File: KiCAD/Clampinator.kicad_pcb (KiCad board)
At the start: 4 copper layers, 200 x 115 mm, 197 parts, among them J1 Power, J10 Conn_01x04, J11 Conn_01x04, J12 FDCAN_1, J13 FDCAN_2, J14 10k NTC, J15 10k NTC, J16 EN_NTC_B, J17 EN_NTC_A, J18 FAN, J19 FAN, J20 VP0265840000G, J23 VP0265840000G, J24 VP0265840000G, J25 +5V INJ, J26 UART4, J5 Debug Header, J6 Conn_01x04, J7 Conn_01x04, J8 Conn_01x04, J9 Conn_01x04, Q1 TK100E10N1,S1X, Q10 AO3400A, Q2 TK100E10N1,S1X, Q3 TK100E10N1,S1X, Q4 TK100E10N1,S1X, Q5 TK100E10N1,S1X, Q9 MMBT3904-C20526, SW1 PTS810SJM250SMTRLFS, SW2 PTS810SJM250SMTRLFS, SW3 PTS810SJM250SMTRLFS, SW4 PTS810SJM250SMTRLFS, SW5 SMQS-02R-TP, SW6 EG1847-ND, SW7 GPI-154-3013, U1 STM32H573RIT6, U10 LM74810QDRRRQ1, U12 TPS7A2033DQNR, U13 VOS618A-3T, U14 LM5163DDAR, U2 TL432BQDBZR, U3 EG2131, U4 UCC33420RAQR_C46461551, U5 USBLC6-2SC6, U6 LM5012DDAR, U7 MCP2562FD-E/P, U8 MCP2562FD-E/P, U9 EL357N, X1 SC-32S32.768kHz20PPM7pF, Y2 ECS-80-18-23B-JTM-TR

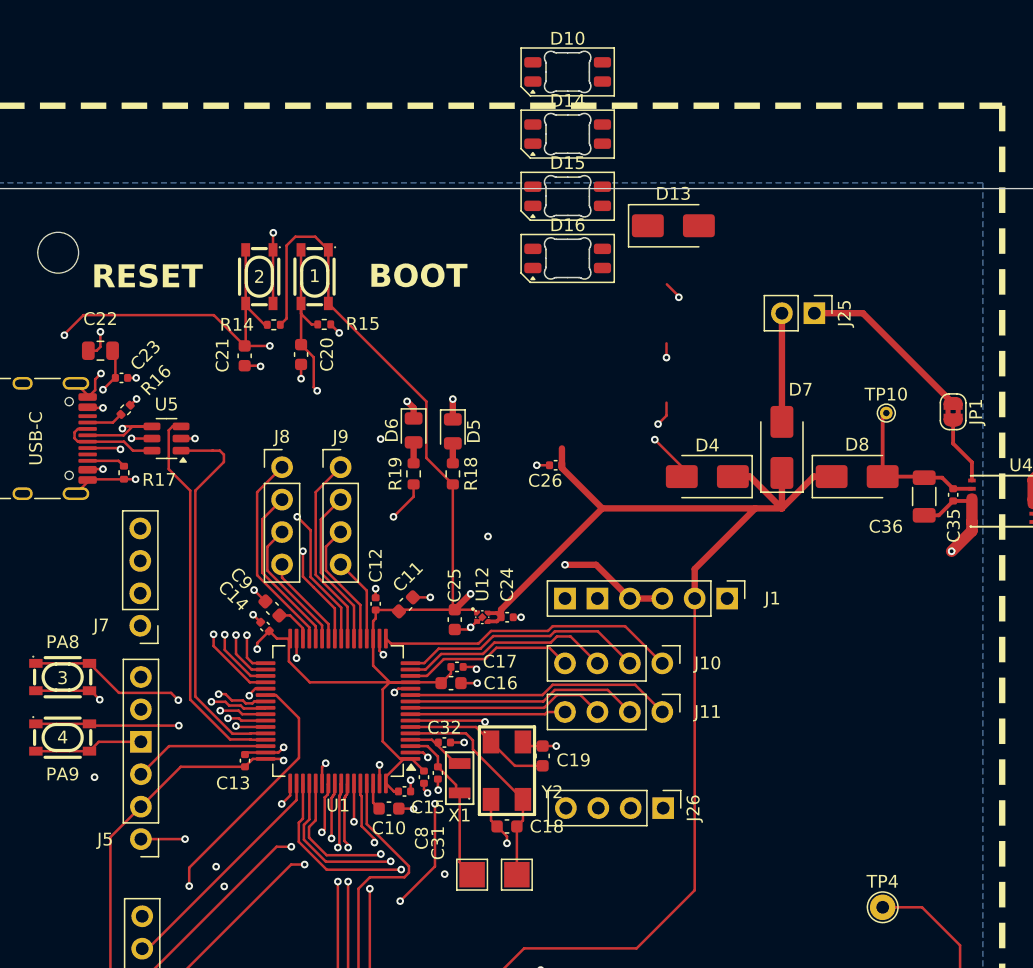
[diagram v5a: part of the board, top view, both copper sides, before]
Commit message: Finish SK7812 layouts + new forward mount footprint from reverse extended leads footprint
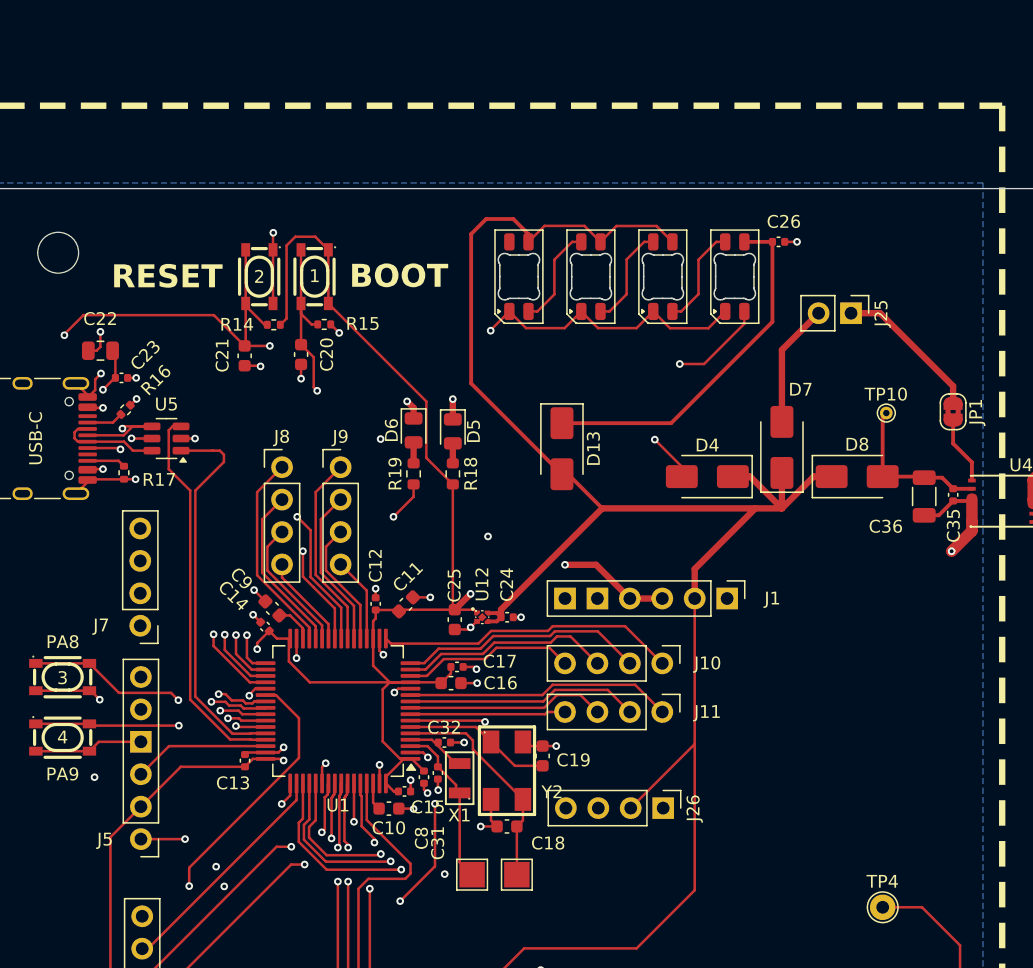
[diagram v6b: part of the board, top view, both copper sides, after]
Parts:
- D10, D14, D15, D16: footprint LED_SMD:LED_SK6812MINI-E_3.2x2.8mm_P1.5mm_ReverseMount -> LED_SMD:LED_SK6812MINI-E_3.2x2.8mm_P1.5mm
- moved C26 24.7 mm to (109.3, 28.7), turned to 0 degrees
- moved D10 20.7 mm to (105.8, 31.4), turned to 90 degrees
- moved D13 19.5 mm to (92.3, 44.9), turned to -90 degrees
- moved D14 13.4 mm to (100.2, 31.4), turned to 90 degrees
- moved D15 6.56 mm to (94.6, 31.4), turned to 90 degrees
- moved D16 4.08 mm to (88.9, 31.4), turned to 90 degrees
- moved J25 2.88 mm to (114.9, 34.3)
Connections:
- C26 pad 1: +5VS -> Net-(D10-VDD)
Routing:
- net +5VS: track 144.5 -> 191.0 mm
- net PC11_RX: track 61.6 -> 27.6 mm, vias 2 -> 1
- net Net-(D10-VDD): track 0.00 -> 28.2 mm
- net PC10_TX: track 58.8 -> 31.1 mm, vias 2 -> 1
- net GND: track 130.9 -> 150.7 mm, vias 37 -> 38
- net Net-(D14-DOUT): track 0.00 -> 7.99 mm
- net Net-(D15-DOUT): track 0.00 -> 7.99 mm
- net Net-(D10-DOUT): track 0.00 -> 7.98 mm
- net PC12_RGB_DIN: track 65.4 -> 69.9 mm
- net Net-(D7-A): track 8.52 -> 9.71 mm

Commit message: Clean up traces
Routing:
- net EN_DIODE_L: track 80.9 -> 76.4 mm, vias 3 -> 2
- net BRAKE_A: track 375.7 -> 379.9 mm
- net PC13: track 41.2 -> 38.6 mm
